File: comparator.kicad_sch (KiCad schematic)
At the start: 8 parts, among them U2 ltc6752ims8-2-pbf

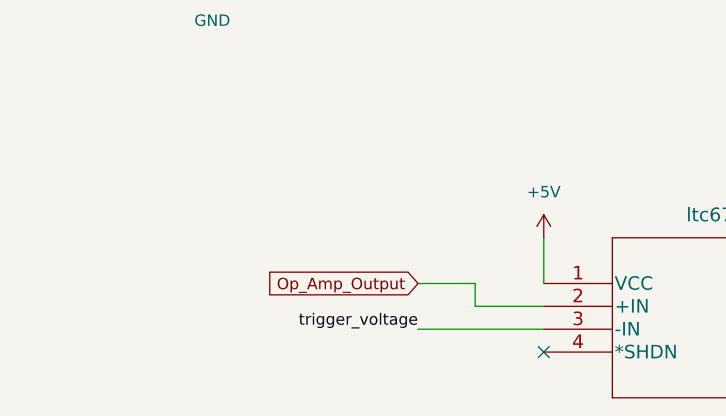
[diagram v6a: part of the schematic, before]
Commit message: Fixed Receiver schematic
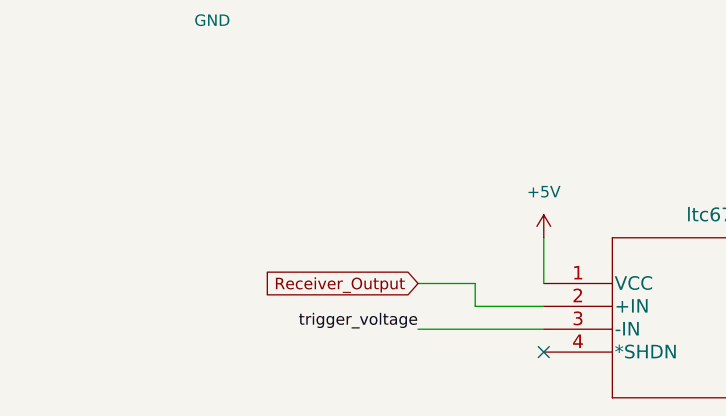
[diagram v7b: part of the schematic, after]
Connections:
- net Op_Amp_Output renamed Receiver_Output
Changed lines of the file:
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@@
     (effects (font (size 1.27 1.27)) (justify left bottom))
   )
-  (global_label "Op_Amp_Output" (shape input) (at 99.06 91.44 180) (fields_autoplaced)
+  (global_label "Receiver_Output" (shape input) (at 99.06 91.44 180) (fields_autoplaced)
     (effects (font (size 1.27 1.27)) (justify right))
-    (property "Intersheet References" "${INTERSHEET_REFS}" (id 0) (at 82.0721 91.3606 0)
+    (property "Intersheet References" "${INTERSHEET_REFS}" (id 0) (at 81.4674 91.3606 0)
       (effects (font (size 1.27 1.27)) (justify right) hide)
     )

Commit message: Resistor and cap footprints (except the ones the store cupboard doesn't have)
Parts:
- C18, C21: footprint (none) -> Capacitor_Tantalum_SMD:CP_EIA-3528-15_AVX-H_Pad1.50x2.35mm_HandSolder
- C19, C20, C22, C23: footprint (none) -> Capacitor_SMD:C_0805_2012Metric_Pad1.18x1.45mm_HandSolder
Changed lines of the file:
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@@
       (effects (font (size 1.27 1.27)) (justify left))
     )
-    (property "Footprint" "" (id 2) (at 159.7152 60.96 0)
+    (property "Footprint" "Capacitor_Tantalum_SMD:CP_EIA-3528-15_AVX-H_Pad1.50x2.35mm_HandSolder" (id 2) (at 159.7152 60.96 0)
       (effects (font (size 1.27 1.27)) hide)
     )
@@
       (effects (font (size 1.27 1.27)) (justify left))
     )
-    (property "Footprint" "" (id 2) (at 173.6852 60.96 0)
+    (property "Footprint" "Capacitor_SMD:C_0805_2012Metric_Pad1.18x1.45mm_HandSolder" (id 2) (at 173.6852 60.96 0)
       (effects (font (size 1.27 1.27)) hide)
     )
@@
       (effects (font (size 1.27 1.27)) (justify left))
     )
-    (property "Footprint" "" (id 2) (at 234.6452 60.96 0)
+    (property "Footprint" "Capacitor_SMD:C_0805_2012Metric_Pad1.18x1.45mm_HandSolder" (id 2) (at 234.6452 60.96 0)
       (effects (font (size 1.27 1.27)) hide)
     )
@@
       (effects (font (size 1.27 1.27)) (justify left))
     )
-    (property "Footprint" "" (id 2) (at 247.3452 60.96 0)
+    (property "Footprint" "Capacitor_SMD:C_0805_2012Metric_Pad1.18x1.45mm_HandSolder" (id 2) (at 247.3452 60.96 0)
       (effects (font (size 1.27 1.27)) hide)
     )
@@
       (effects (font (size 1.27 1.27)) (justify left))
     )
-    (property "Footprint" "" (id 2) (at 186.3852 60.96 0)
+    (property "Footprint" "Capacitor_SMD:C_0805_2012Metric_Pad1.18x1.45mm_HandSolder" (id 2) (at 186.3852 60.96 0)
       (effects (font (size 1.27 1.27)) hide)
     )
@@
       (effects (font (size 1.27 1.27)) (justify left))
     )
-    (property "Footprint" "" (id 2) (at 220.6752 60.96 0)
+    (property "Footprint" "Capacitor_Tantalum_SMD:CP_EIA-3528-15_AVX-H_Pad1.50x2.35mm_HandSolder" (id 2) (at 220.6752 60.96 0)
       (effects (font (size 1.27 1.27)) hide)
     )
